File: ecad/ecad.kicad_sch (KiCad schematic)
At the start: 17 parts, among them J1 Raspberry_Pi_2_3, Q1 BC547, Q4 BC547, SW1 SW_DPST

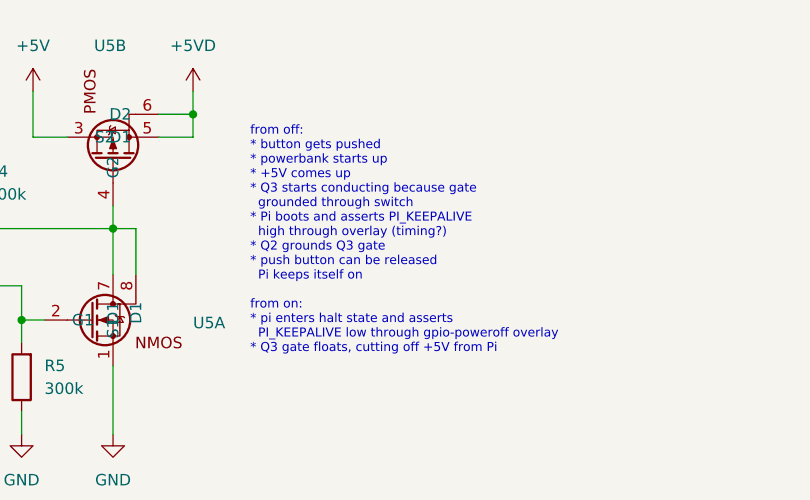
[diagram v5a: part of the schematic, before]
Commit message: update power circuit description
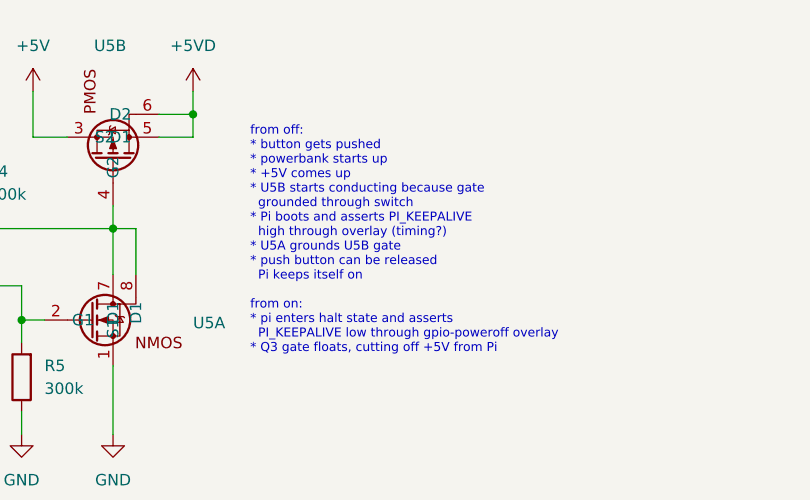
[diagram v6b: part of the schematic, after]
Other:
- note added: "from off: * button gets pushed * powerbank starts up * +5V comes up * U5B starts conducting because gate grounded through switch * Pi boots and asserts PI_KEEPALIVE high through overlay (timing?) * U5A grounds U5B gate * push button can be released Pi keeps itself on from on: * pi enters halt state and asserts PI_KEEPALIVE low through gpio-poweroff overlay * Q3 gate floats, cutting off +5V from Pi"
- note removed: "from off: * button gets pushed * powerbank starts up * +5V comes up * Q3 starts conducting because gate grounded through switch * Pi boots and asserts PI_KEEPALIVE high through overlay (timing?) * Q2 grounds Q3 gate * push button can be released Pi keeps itself on from on: * pi enters halt state and asserts PI_KEEPALIVE low through gpio-poweroff overlay * Q3 gate floats, cutting off +5V from Pi"
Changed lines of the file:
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@@
     (stroke (width 0) (type default))
   )
-  (text "from off:\n* button gets pushed\n* powerbank starts up\n* +5V comes up\n* Q3 starts conducting because gate\n  grounded through switch\n* Pi boots and asserts PI_KEEPALIVE\n  high through overlay (timing?)\n* Q2 grounds Q3 gate\n* push button can be released\n  Pi keeps itself on\n\nfrom on:\n* pi enters halt state and asserts\n  PI_KEEPALIVE low through gpio-poweroff overlay\n* Q3 gate floats, cutting off +5V from Pi"
+  (text "from off:\n* button gets pushed\n* powerbank starts up\n* +5V comes up\n* U5B starts conducting because gate\n  grounded through switch\n* Pi boots and asserts PI_KEEPALIVE\n  high through overlay (timing?)\n* U5A grounds U5B gate\n* push button can be released\n  Pi keeps itself on\n\nfrom on:\n* pi enters halt state and asserts\n  PI_KEEPALIVE low through gpio-poweroff overlay\n* Q3 gate floats, cutting off +5V from Pi"
     (at 194.31 57.15 0)
     (effects (font (size 1 1)) (justify left bottom))

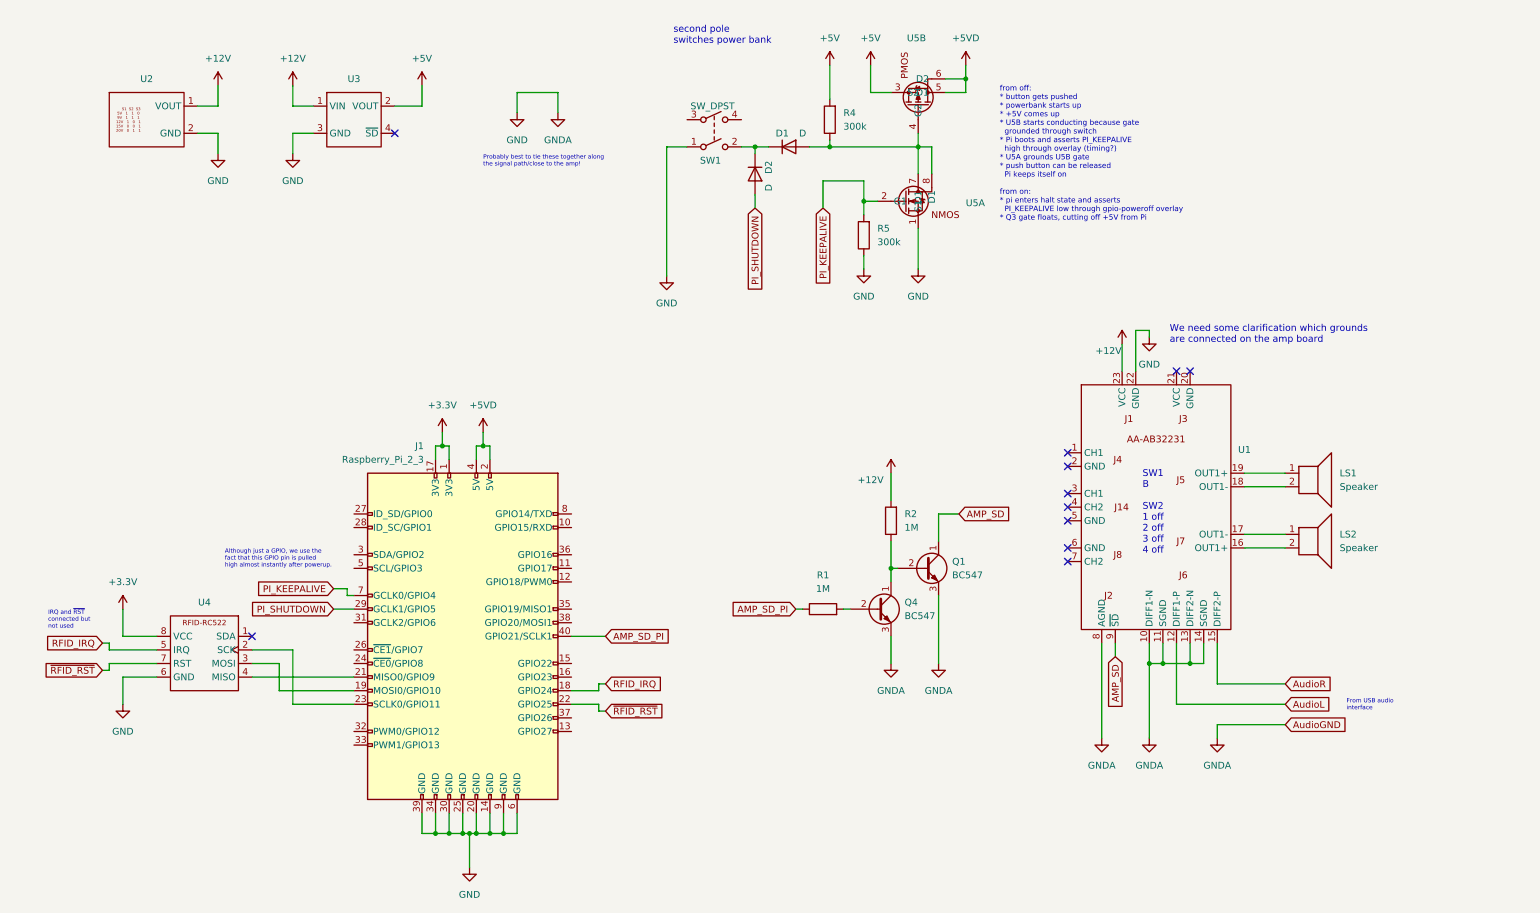
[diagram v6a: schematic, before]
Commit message: update power management
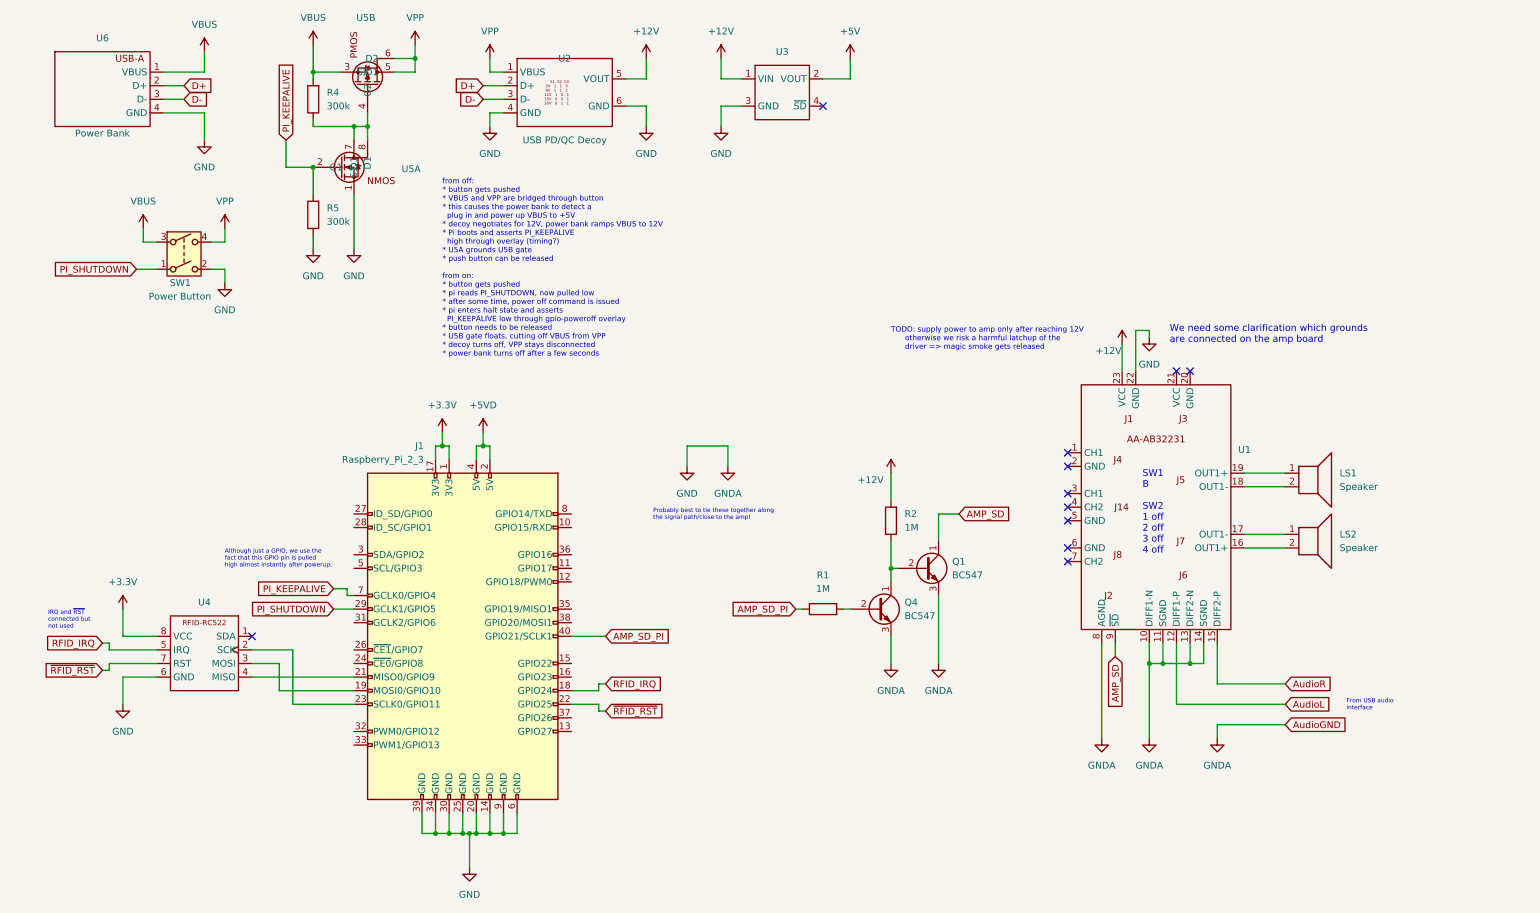
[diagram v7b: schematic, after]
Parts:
- removed D1, D2: D, symbol Device:D
- added U6: Power Bank, symbol drempelbox:PowerBank
- SW1: value SW_DPST -> Power Button
- U2: value ~ -> USB PD/QC Decoy
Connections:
- net +12V: now also U2.5 (VOUT); no longer U2.1 (VOUT)
- net +5V: no longer R4.2, U5.3 (S2)
- net +5VD: no longer U5.5 (D1), U5.6 (D2)
- net GND: now also SW1.2, U2.4 (GND), U2.6 (GND), U6.4 (GND); no longer SW1.1, U2.2 (GND)
- net PI_SHUTDOWN: now also SW1.1
- net VBUS: now reaches SW1.3
- net VBUS: now also R4.2, U5.3 (S2), U6.1 (VBUS)
- net VPP: now reaches SW1.4
- net VPP: now also U2.1 (VBUS), U5.5 (D1), U5.6 (D2)
- new net D+: U2.2 (D+), U6.2 (D+)
- new net D-: U2.3 (D-), U6.3 (D-)
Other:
- note added: "TODO: supply power to amp only after reaching 12V otherwise we risk a harmful latchup of the driver => magic smoke gets released"
- note added: "from off: * button gets pushed * VBUS and VPP are bridged through button * this causes the power bank to detect a plug in and power up VBUS to +5V * decoy negotiates for 12V, power bank ramps VBUS to 12V * Pi boots and asserts PI_KEEPALIVE high through overlay (timing?) * U5A grounds U5B gate * push button can be released from on: * button gets pushed * pi reads PI_SHUTDOWN, now pulled low * afte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"
- note removed: "from off: * button gets pushed * powerbank starts up * +5V comes up * U5B starts conducting because gate grounded through switch * Pi boots and asserts PI_KEEPALIVE high through overlay (timing?) * U5A grounds U5B gate * push button can be released Pi keeps itself on from on: * pi enters halt state and asserts PI_KEEPALIVE low through gpio-poweroff overlay * Q3 gate floats, cutting off +5V from Pi"
- note removed: "second pole switches power bank"
- moved on the sheet: R4, R5, U3, U5A, U5B

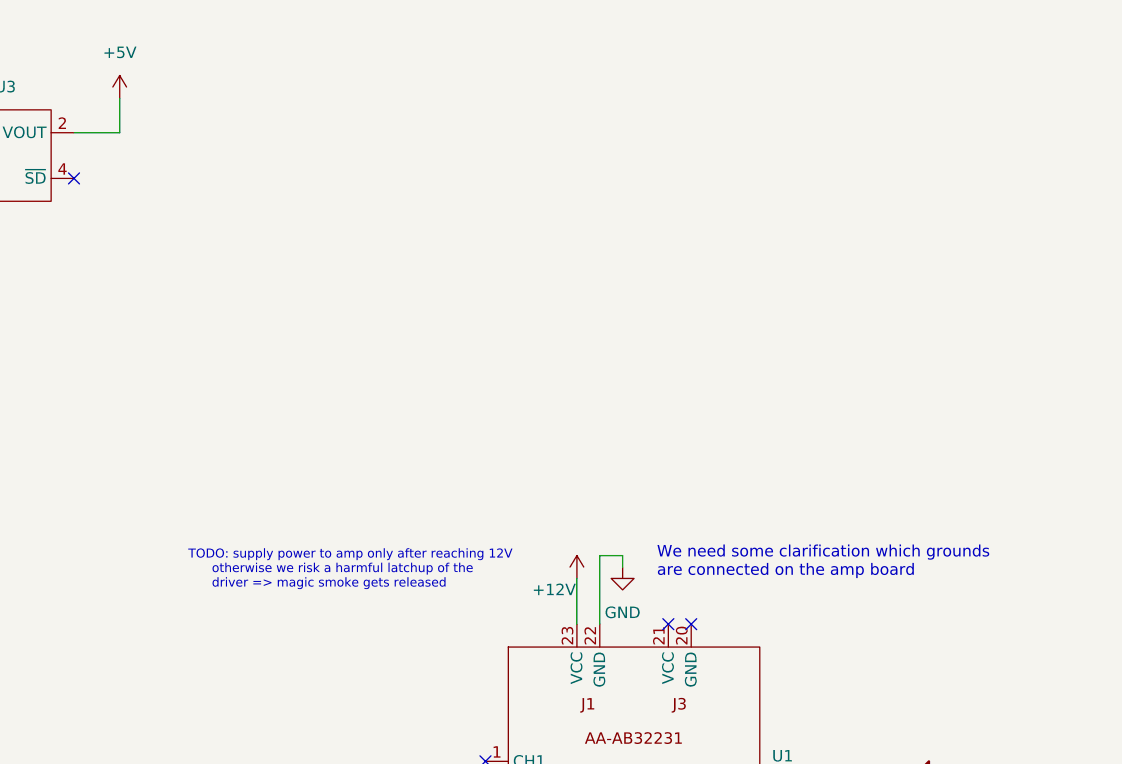
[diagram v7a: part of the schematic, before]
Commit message: added amp power switching
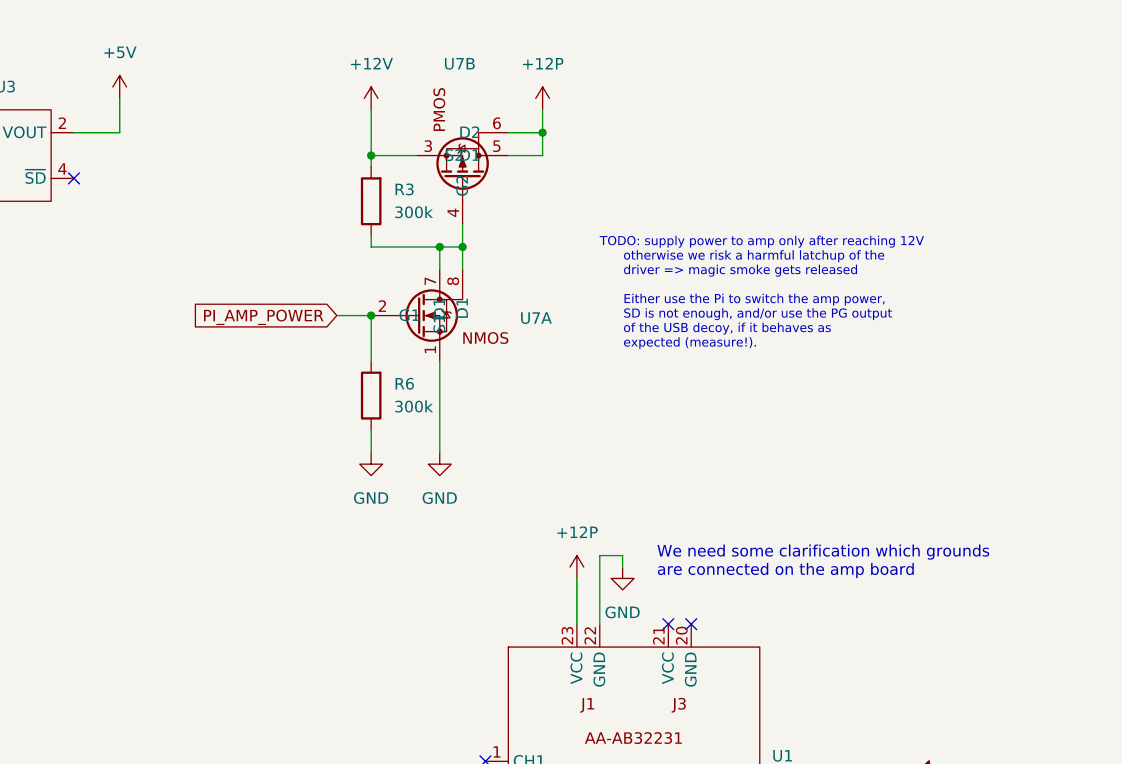
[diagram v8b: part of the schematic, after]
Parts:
- added R3, R6: 300k, symbol Device:R
- added U7: ~, symbol drempelbox:IRF7319
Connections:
- net +12V: now also R3.2, U7.3 (S2); no longer U1.23 (VCC)
- net GND: now also R6.1, U7.1 (S1)
- new net: R3.1, U7.4 (G2), U7.7 (D1), U7.8 (D1)
- new net +12P: U1.23 (VCC), U7.5 (D1), U7.6 (D2)
- new net PI_AMP_POWER: R6.2, U7.2 (G1)
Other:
- note added: "TODO: supply power to amp only after reaching 12V otherwise we risk a harmful latchup of the driver => magic smoke gets released Either use the Pi to switch the amp power, SD is not enough, and/or use the PG output of the USB decoy, if it behaves as expected (measure!)."
- note removed: "TODO: supply power to amp only after reaching 12V otherwise we risk a harmful latchup of the driver => magic smoke gets released"
